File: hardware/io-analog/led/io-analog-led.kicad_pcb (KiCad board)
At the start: 2 copper layers, 60 x 60 mm, 17 parts, among them J1 Input, J2 Output, J3 Power, J4 Power, J5 C Out, J6 D Out, Q1 FQP30N06L, Q2 FQP30N06L

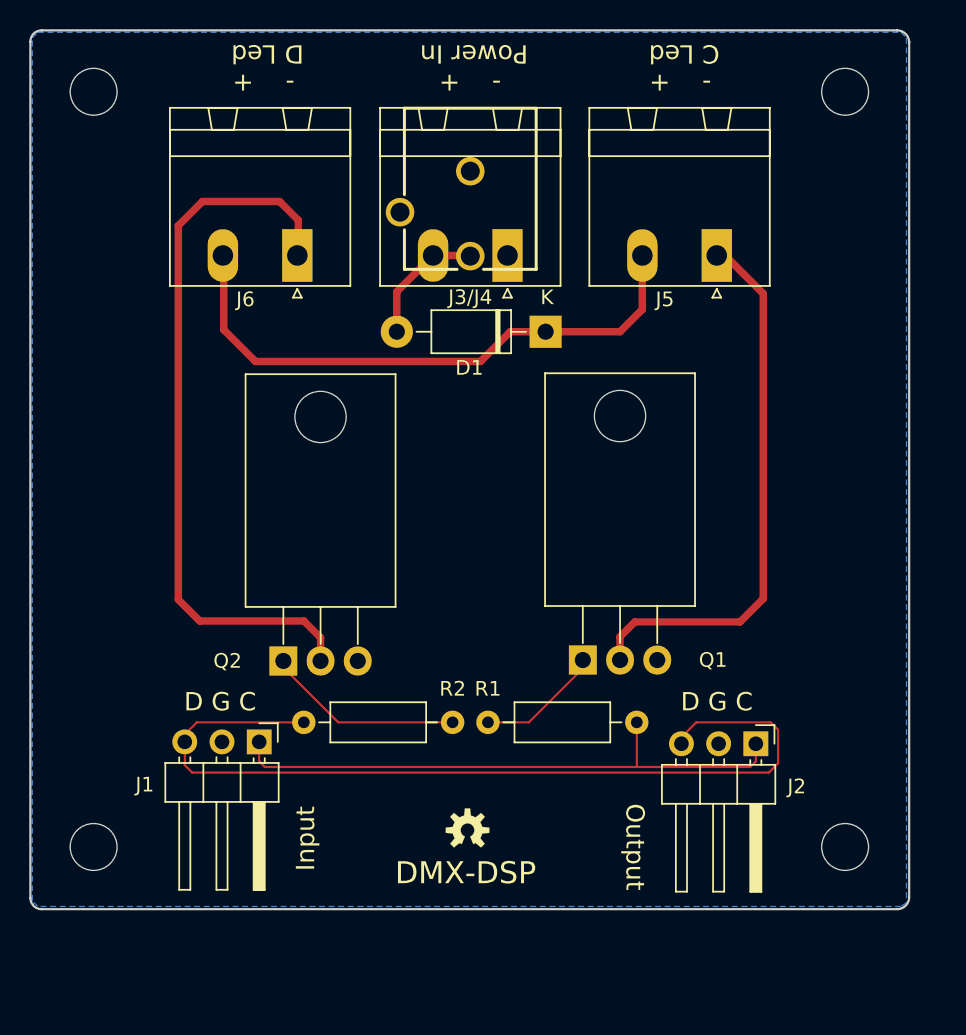
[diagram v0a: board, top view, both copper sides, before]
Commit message: Make io-analog a stackable family io-analog-core handles D to A io-analog-amplify handles voltage output io-analog-pwm handles pwm output for leds, drive display pro io-analog-led handles 5v pwm output for iot, drive display pro
Refactor display-pro to work with io-analog-pwm
Add correct coax power connector
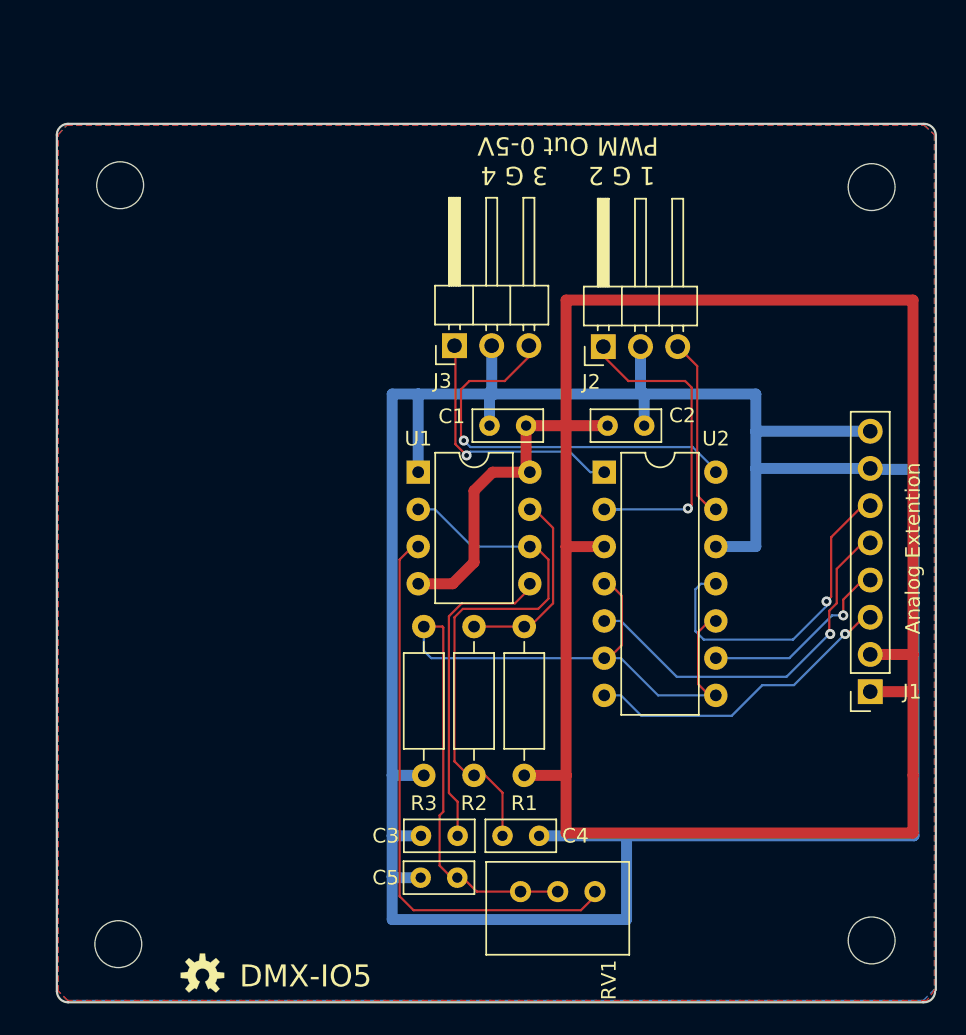
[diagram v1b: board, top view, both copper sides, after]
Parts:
- removed the ? at (144.3, 115.2)
- removed D1: 1N5819, Diode_THT:D_DO-41_SOD81_P10.16mm_Horizontal
- removed J4: Power, POWER_JACK_PTH_BREAD
- removed J5: C Out, Connector_Phoenix_MSTB:PhoenixContact_MSTBA_2,5_2-G-5,08_1x02_P5.08mm_Horizontal
- removed J6: D Out, Connector_Phoenix_MSTB:PhoenixContact_MSTBA_2,5_2-G-5,08_1x02_P5.08mm_Horizontal
- removed Q1, Q2: FQP30N06L, Package_TO_SOT_THT:TO-220-3_Horizontal_TabDown
- added ?: , footprints:OSHW-LOGO-S, F.Cu at (126.2, 125.1)
- added C1: 0.1uF, Capacitor_THT:C_Rect_L4.6mm_W2.0mm_P2.50mm_MKS02_FKP02, F.Cu at (148.3, 87.6)
- added C2: 0.1uF, Capacitor_THT:C_Rect_L4.6mm_W2.0mm_P2.50mm_MKS02_FKP02, F.Cu at (153.8, 87.6)
- added C3: 100nf, Capacitor_THT:C_Rect_L4.6mm_W2.0mm_P2.50mm_MKS02_FKP02, F.Cu at (141.1, 115.6)
- added C4: 0.68uF, Capacitor_THT:C_Rect_L4.6mm_W2.0mm_P2.50mm_MKS02_FKP02, F.Cu at (149.2, 115.6)
- added C5: 0.68uF, Capacitor_THT:C_Rect_L4.6mm_W2.0mm_P2.50mm_MKS02_FKP02, F.Cu at (143.6, 118.4)
- added R3: 10k, Resistor_THT:R_Axial_DIN0207_L6.3mm_D2.5mm_P10.16mm_Horizontal, F.Cu at (141.3, 111.4)
- added RV1: 10k, Potentiometer_THT:Potentiometer_Bourns_3299W_Vertical, F.Cu at (153.0, 119.4)
- added U1: LM555, Package_DIP:DIP-8_W7.62mm, F.Cu at (140.9, 90.7)
- added U2: LM339, Package_DIP:DIP-14_W7.62mm, F.Cu at (153.6, 90.7)
- J1: value Input -> Analog Extension; footprint Connector_PinHeader_2.54mm:PinHeader_1x03_P2.54mm_Horizontal -> Connector_PinSocket_2.54mm:PinSocket_1x08_P2.54mm_Vertical
- J2: value Output -> PWM Out 1/2
- J3: value Power -> PWM Out 3/4; footprint Connector_Phoenix_MSTB:PhoenixContact_MSTBA_2,5_2-G-5,08_1x02_P5.08mm_Horizontal -> Connector_PinHeader_2.54mm:PinHeader_1x03_P2.54mm_Horizontal
- R1: value 10k -> 330
- moved J1 41.9 mm to (171.8, 105.7), turned to 180 degrees
- moved J2 29.0 mm to (153.5, 82.2), turned to 90 degrees
- moved G*** 9.05 mm to (127.0, 122.5)
- moved J3 7.14 mm to (143.4, 82.1), turned to 90 degrees
- moved MH3 6.84 mm to (120.4, 123.0), turned to 0 degrees
- moved MH2 6.75 mm to (171.9, 71.3)
- moved R2 6.70 mm to (144.7, 101.3), turned to 270 degrees
- moved MH4 6.63 mm to (171.9, 122.7), turned to 0 degrees
- moved MH1 6.63 mm to (120.6, 71.2)
- moved R1 4.39 mm to (148.1, 111.4), turned to 90 degrees
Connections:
- J1 pad 1: /C -> +5V
- J1 pad 2: GND -> +5V
- J1 pad 3: /D -> /AO3
- J2 pad 1: /C -> Net-(J2-Pad1)
- J2 pad 3: /D -> Net-(J2-Pad3)
- J3 pad 1: GND -> Net-(J3-Pad1)
- J3 pad 2: Net-(D1-Pad2) -> GND
- R1 pad 1: Net-(Q1-Pad1) -> +5V
- R1 pad 2: /C -> Net-(R1-Pad2)
- R2 pad 1: Net-(Q2-Pad1) -> Net-(R1-Pad2)
- R2 pad 2: /D -> Net-(C4-Pad2)
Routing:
- net GND: track 0.00 -> 187.4 mm
- net +5V: track 0.00 -> 154.2 mm
- net Net-(C5-Pad1): track 0.00 -> 62.5 mm
- net /D: track 61.5 -> 0.00 mm
- net Net-(J6-Pad1): track 49.7 -> 0.00 mm
- net /C: track 39.8 -> 0.00 mm
- net +VDC: track 39.7 -> 0.00 mm
- net Net-(RV1-Pad1): track 0.00 -> 39.1 mm
- net Net-(J5-Pad1): track 37.5 -> 0.00 mm
- net Net-(C4-Pad2): track 0.00 -> 36.9 mm
- net Net-(J3-Pad3): track 0.00 -> 28.0 mm, vias 0 -> 1
- net /AO1: track 0.00 -> 25.9 mm, vias 0 -> 1
- net /AO0: track 0.00 -> 22.9 mm, vias 0 -> 1
- net Net-(J2-Pad1): track 0.00 -> 22.8 mm, vias 0 -> 1
- net Net-(C3-Pad2): track 0.00 -> 21.9 mm
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- added copper zone on F.Cu, net +5V
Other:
- outline, holes or cut-outs redrawn
- net class 1Amp removed
- net class Power added: clearance 0.25, trace_width 0.75, via_dia 1.27, via_drill 0.635
- rule pad_to_mask_clearance: 0.0508 -> 0.2
- board text added: "1 G 2 3 G 4 PWM Out 0-5V"
- board text added: "Analog Extention"
- board text added: "DMX-IO5"
- board text added: "DMX-IO5, Rev 1.2 Crazy Giraffe Software"
- board text removed: "- + C Led"
- board text removed: "- + D Led"
- board text removed: "- + Power In"
- board text removed: "D G C"
- board text removed: "DMX-DSP"
- board text removed: "DMX-DSP, Rev 1.4 Crazy Giraffe Software"
- board text removed: "Input"
- board text removed: "J3/J4"
- board text removed: "Output"
